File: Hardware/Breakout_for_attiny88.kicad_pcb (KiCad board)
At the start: 2 copper layers, 22.9 x 48.5 mm, 12 parts, among them J1 HEADER, J2 HEADER, J3 AVR-ISP-6, J4 PWR, SW1 SW, U1 ATtiny88

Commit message: add filled zone on both sides.
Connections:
- SW1 pad 3: (no net) -> GND
- SW1 pad 4: (no net) -> GND
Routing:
- net PC6: track 63.4 -> 57.4 mm, vias 0 -> 1
- added copper zone on B.Cu, net GND
- added copper zone on F.Cu, net GND
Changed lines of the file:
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@@
     (property "Sheet name" "")
     (attr through_hole)
-    (fp_text reference "SW1" (at 5.80644 0.0127 90) (layer "F.SilkS")
+    (fp_text reference "SW1" (at 0.48 -3.71 180) (layer "F.SilkS")
       (effects (font (size 1 1) (thickness 0.15)))
     )
@@
       (net 17 "PC6") (pinfunction "2") (solder_mask_margin 0.000254))
     (pad "3" smd rect (at -3.2 -2.075 180) (size 1 1.15) (layers "F.Cu" "F.Paste" "F.Mask")
-      (solder_mask_margin 0.000254))
+      (net 1 "GND") (solder_mask_margin 0.000254))
     (pad "4" smd rect (at 3.2 2.075 180) (size 1 1.15) (layers "F.Cu" "F.Paste" "F.Mask")
-      (solder_mask_margin 0.000254))
+      (net 1 "GND") (solder_mask_margin 0.000254))
     (model "${KISYS3DMOD}/Button_Switch_SMD.3dshapes/SW_SPST_CK_RS282G05A3.wrl"
       (offset (xyz 0 0 0))
@@
     (property "Sheet name" "")
     (attr smd)
-    (fp_text reference "C1" (at 0 1.68 270) (layer "B.SilkS")
+    (fp_text reference "C1" (at 0.965 -2.075) (layer "B.SilkS")
       (effects (font (size 1 1) (thickness 0.15)) (justify mirror))
     )
@@
     (property "Sheet name" "")
     (attr smd)
-    (fp_text reference "R1" (at 0 1.65 180) (layer "B.SilkS")
+    (fp_text reference "R1" (at 3.62 0.01 180) (layer "B.SilkS")
       (effects (font (size 1 1) (thickness 0.15)) (justify mirror))
     )
@@
   (gr_line (start 137.07 77.86518) (end 137.07 126.3868) (layer "Edge.Cuts") (width 0.05))
   (gr_line (start 159.93 77.86518) (end 159.93 126.3868) (layer "Edge.Cuts") (width 0.05))
-  (gr_text "PB3" (at 154.44614 93.62842) (layer "F.SilkS")
-    (effects (font (size 1 1) (thickness 0.15)))
-  )
-  (gr_text "PB2" (at 154.44614 96.16842) (layer "F.SilkS")
-    (effects (font (size 1 1) (thickness 0.15)))
-  )
-  (gr_text "PB1" (at 154.44614 98.70842) (layer "F.SilkS")
-    (effects (font (size 1 1) (thickness 0.15)))
-  )
-  (gr_text "PB0" (at 154.44614 101.24842) (layer "F.SilkS")
-    (effects (font (size 1 1) (thickness 0.15)))
-  )
-  (gr_text "PD7" (at 154.44614 103.78842) (layer "F.SilkS")
-    (effects (font (size 1 1) (thickness 0.15)))
-  )
-  (gr_text "PD6" (at 154.44614 106.32842) (layer "F.SilkS")
-    (effects (font (size 1 1) (thickness 0.15)))
-  )
-  (gr_text "PD5" (at 154.44614 108.86842) (layer "F.SilkS")
-    (effects (font (size 1 1) (thickness 0.15)))
-  )
-  (gr_text "PB7" (at 154.44614 111.40842) (layer "F.SilkS")
-    (effects (font (size 1 1) (thickness 0.15)))
-  )
-  (gr_text "PB6" (at 154.44614 113.94842) (layer "F.SilkS")
-    (effects (font (size 1 1) (thickness 0.15)))
-  )
-  (gr_text "PD4" (at 154.44614 116.48842) (layer "F.SilkS")
-    (effects (font (size 1 1) (thickness 0.15)))
-  )
-  (gr_text "PD3" (at 154.44614 119.02842) (layer "F.SilkS")
-    (effects (font (size 1 1) (thickness 0.15)))
+  (gr_text "PB3" (at 154.63 93.62842) (layer "F.SilkS")
+    (effects (font (size 0.8 0.8) (thickness 0.15)))
+  )
+  (gr_text "PB2" (at 154.63 96.16842) (layer "F.SilkS")
+    (effects (font (size 0.8 0.8) (thickness 0.15)))
+  )
+  (gr_text "PB1" (at 154.63 98.70842) (layer "F.SilkS")
+    (effects (font (size 0.8 0.8) (thickness 0.15)))
+  )
+  (gr_text "PB0" (at 154.63 101.24842) (layer "F.SilkS")
+    (effects (font (size 0.8 0.8) (thickness 0.15)))
+  )
+  (gr_text "PD7" (at 154.63 103.78842) (layer "F.SilkS")
+    (effects (font (size 0.8 0.8) (thickness 0.15)))
+  )
+  (gr_text "PD6" (at 154.63 106.32842) (layer "F.SilkS")
+    (effects (font (size 0.8 0.8) (thickness 0.15)))
+  )
+  (gr_text "PD5" (at 154.63 108.86842) (layer "F.SilkS")
+    (effects (font (size 0.8 0.8) (thickness 0.15)))
+  )
+  (gr_text "PB7" (at 154.63 111.40842) (layer "F.SilkS")
+    (effects (font (size 0.8 0.8) (thickness 0.15)))
+  )
+  (gr_text "PB6" (at 154.63 113.94842) (layer "F.SilkS")
+    (effects (font (size 0.8 0.8) (thickness 0.15)))
+  )
+  (gr_text "PD4" (at 154.63 116.48842) (layer "F.SilkS")
+    (effects (font (size 0.8 0.8) (thickness 0.15)))
+  )
+  (gr_text "PD3" (at 154.63 119.02842) (layer "F.SilkS")
+    (effects (font (size 0.8 0.8) (thickness 0.15)))
   )
   (gr_text "PC2" (at 142.52084 101.41352) (layer "F.SilkS")
@@
     (effects (font (size 1 1) (thickness 0.15)))
   )
-  (gr_text "PB4" (at 154.44614 91.08842) (layer "F.SilkS")
-    (effects (font (size 1 1) (thickness 0.15)))
+  (gr_text "PB4" (at 154.63 91.08842) (layer "F.SilkS")
+    (effects (font (size 0.8 0.8) (thickness 0.15)))
   )
   (segment (start 144.2548 86.6402) (end 144.2548 93.2323) (width 0.2) (layer "F.Cu") (net 1))
@@
   (segment (start 145.82 107.68) (end 147.121142 106.378858) (width 0.2) (layer "F.Cu") (net 17))
   (segment (start 139.61 111.35) (end 142.98 111.35) (width 0.2) (layer "F.Cu") (net 17))
-  (segment (start 138.36 116.97) (end 139 117.61) (width 0.2) (layer "F.Cu") (net 17))
-  (segment (start 139.61 111.35) (end 138.36 112.6) (width 0.2) (layer "F.Cu") (net 17))
-  (segment (start 139 117.61) (end 143.9203 117.61) (width 0.2) (layer "F.Cu") (net 17))
-  (segment (start 138.36 112.6) (end 138.36 116.97) (width 0.2) (layer "F.Cu") (net 17))
-  (segment (start 143.9203 117.61) (end 144.6 116.9303) (width 0.2) (layer "F.Cu") (net 17))
-  (segment (start 144.6 116.9303) (end 144.6 116.03) (width 0.2) (layer "F.Cu") (net 17))
+  (segment (start 142.74 116.03) (end 144.6 116.03) (width 0.2) (layer "F.Cu") (net 17))
+  (via (at 142.74 116.03) (size 0.5) (drill 0.3) (layers "F.Cu" "B.Cu") (net 17))
   (segment (start 143.19 85.165) (end 145.965 82.39) (width 0.2) (layer "B.Cu") (net 17))
   (segment (start 143.19 107.78) (end 143.19 85.165) (width 0.2) (layer "B.Cu") (net 17))
@@
   (segment (start 139.62 111.35) (end 143.19 107.78) (width 0.2) (layer "B.Cu") (net 17))
   (segment (start 139.61 111.35) (end 139.62 111.35) (width 0.2) (layer "B.Cu") (net 17))
+  (segment (start 142.74 114.48) (end 142.74 116.03) (width 0.2) (layer "B.Cu") (net 17))
   (segment (start 147.18 101.96) (end 147.18 102.861) (width 0.2) (layer "B.Cu") (net 17))
   (segment (start 145.811 104.23) (end 143.19 104.23) (width 0.2) (layer "B.Cu") (net 17))
   (segment (start 149.5 99.92) (end 149.5 99.93) (width 0.2) (layer "B.Cu") (net 17))
+  (segment (start 139.61 111.35) (end 142.74 114.48) (width 0.2) (layer "B.Cu") (net 17))
   (segment (start 148.18 101.6779) (end 148.18 101.66) (width 0.2) (layer "F.Cu") (net 18))
   (segment (start 147.7575 102.9847) (end 147.3154 102.5425) (width 0.2) (layer "F.Cu") (net 18))
@@
   (segment (start 145.9372 106.29) (end 146.4847 105.7425) (width 0.2) (layer "F.Cu") (net 29))
   (segment (start 139.61 106.27) (end 139.63 106.29) (width 0.2) (layer "F.Cu") (net 29))
+  (zone (net 1) (net_name "GND") (layer "F.Cu") (name "GroundPlane") (hatch edge 0.508)
+    (connect_pads (clearance 0.508))
+    (min_thickness 0.254) (filled_areas_thickness no)
+    (fill yes (thermal_gap 0.508) (thermal_bridge_width 0.508))
+    (polygon
+      (pts
+        (xy 159.904828 126.361646)
+        (xy 137.095059 126.361702)
+        (xy 137.095171 77.890331)
+        (xy 159.904892 77.890314)
+      )
+    )
+  )
+  (zone (net 1) (net_name "GND") (layer "B.Cu") (name "GroundPlane") (hatch edge 0.508)
+    (connect_pads (clearance 0.508))
+    (min_thickness 0.254) (filled_areas_thickness no)
+    (fill yes (thermal_gap 0.508) (thermal_bridge_width 0.508))
+    (polygon
+      (pts
+        (xy 159.904828 126.35133)
+        (xy 137.095059 126.351386)
+        (xy 137.095171 77.880015)
+        (xy 159.904892 77.879998)
+      )
+    )
+  )
 )

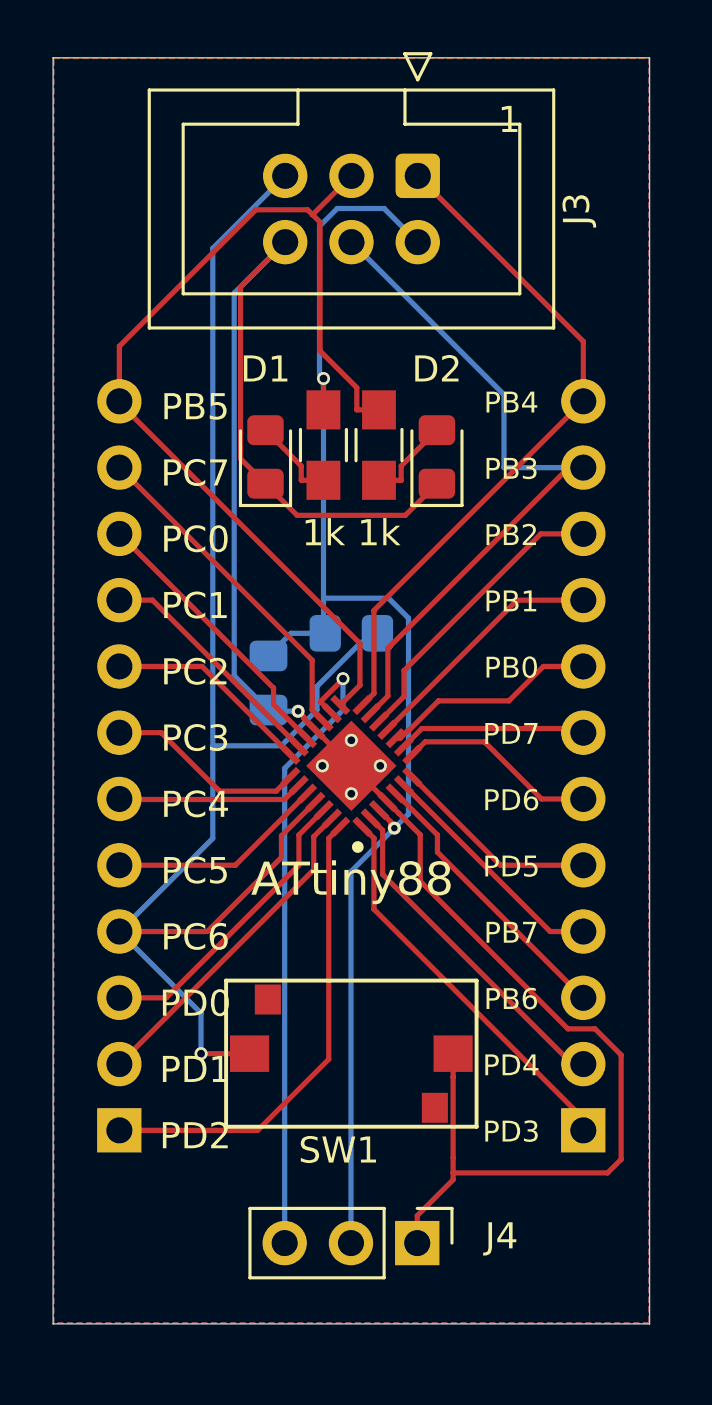
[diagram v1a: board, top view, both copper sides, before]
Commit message: modified Ground plane
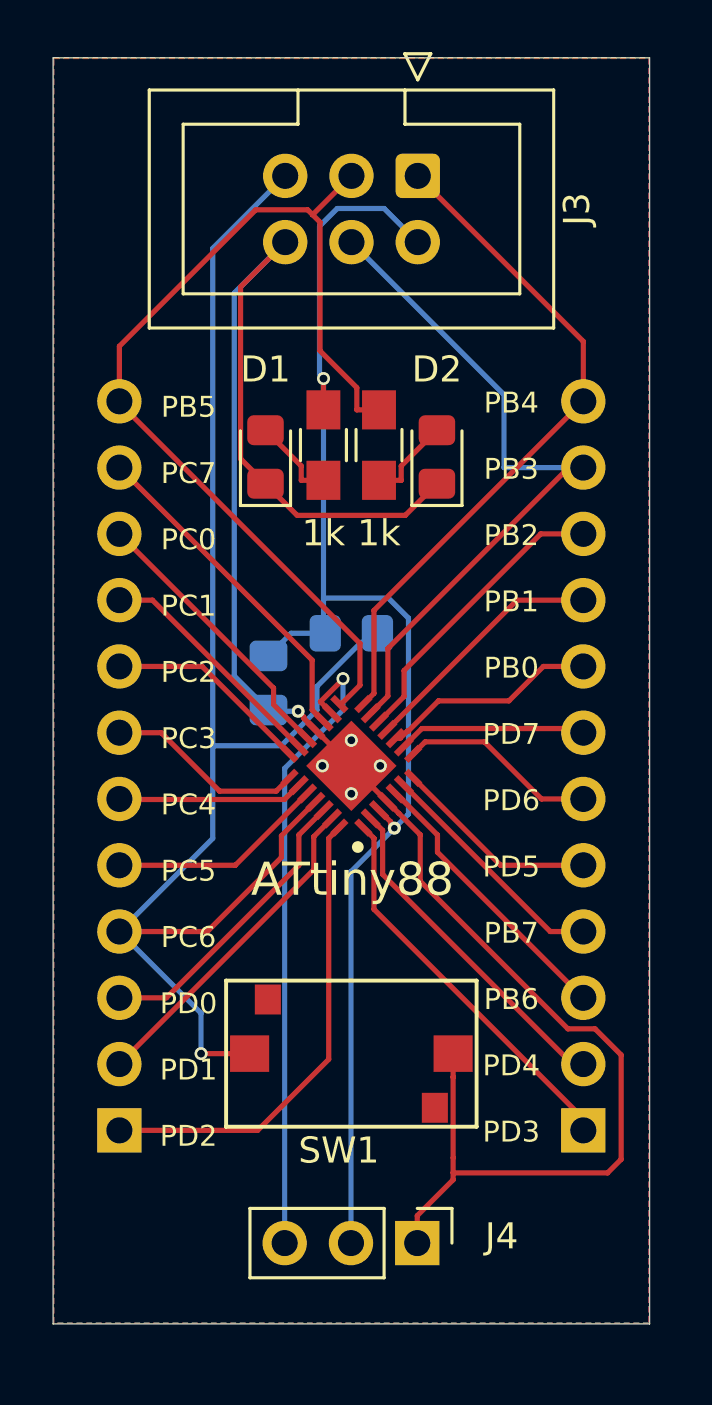
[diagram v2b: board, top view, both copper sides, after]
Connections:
- SW1 pad 4: GND -> (no net)
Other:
- board text removed: "1"
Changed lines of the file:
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@@
   )
   (setup
+    (stackup
+      (layer "F.SilkS" (type "Top Silk Screen"))
+      (layer "F.Paste" (type "Top Solder Paste"))
+      (layer "F.Mask" (type "Top Solder Mask") (color "Green") (thickness 0.01))
+      (layer "F.Cu" (type "copper") (thickness 0.035))
+      (layer "dielectric 1" (type "core") (thickness 1.51) (material "FR4") (epsilon_r 4.5) (loss_tangent 0.02))
+      (layer "B.Cu" (type "copper") (thickness 0.035))
+      (layer "B.Mask" (type "Bottom Solder Mask") (color "Green") (thickness 0.01))
+      (layer "B.Paste" (type "Bottom Solder Paste"))
+      (layer "B.SilkS" (type "Bottom Silk Screen"))
+      (copper_finish "None")
+      (dielectric_constraints no)
+    )
     (grid_origin 148.5 105)
     (pcbplotparams
@@
       (net 1 "GND") (solder_mask_margin 0.000254))
     (pad "4" smd rect (at 3.2 2.075 180) (size 1 1.15) (layers "F.Cu" "F.Paste" "F.Mask")
-      (net 1 "GND") (solder_mask_margin 0.000254))
+      (solder_mask_margin 0.000254))
     (model "${KISYS3DMOD}/Button_Switch_SMD.3dshapes/SW_SPST_CK_RS282G05A3.wrl"
       (offset (xyz 0 0 0))
@@
     )
     (fp_circle (center -2.3745 -2.025) (end -2.3745 -1.9125) (layer "F.SilkS") (width 0.225) (fill none))
+    (fp_line (start -2.625 2.625) (end -2.625 -2.625) (layer "F.CrtYd") (width 0.05))
     (fp_line (start -2.625 -2.625) (end 2.625 -2.625) (layer "F.CrtYd") (width 0.05))
-    (fp_line (start -2.625 2.625) (end -2.625 -2.625) (layer "F.CrtYd") (width 0.05))
     (fp_line (start 2.625 -2.625) (end 2.625 2.625) (layer "F.CrtYd") (width 0.05))
     (fp_line (start 2.625 2.625) (end -2.625 2.625) (layer "F.CrtYd") (width 0.05))
+    (fp_line (start -2 2) (end -2 -2) (layer "F.Fab") (width 0.1))
+    (fp_line (start 2 -2) (end 2 2) (layer "F.Fab") (width 0.1))
+    (fp_line (start -2 -1.55) (end -1.55 -2) (layer "F.Fab") (width 0.1))
     (fp_line (start 2 2) (end -2 2) (layer "F.Fab") (width 0.1))
-    (fp_line (start -2 -1.55) (end -1.55 -2) (layer "F.Fab") (width 0.1))
-    (fp_line (start -2 2) (end -2 -2) (layer "F.Fab") (width 0.1))
     (fp_line (start -2 -2) (end 2 -2) (layer "F.Fab") (width 0.1))
-    (fp_line (start 2 -2) (end 2 2) (layer "F.Fab") (width 0.1))
-    (pad "1" smd rect (at -1.95 -1.35 225) (size 0.25 0.85) (layers "F.Cu" "F.Paste" "F.Mask")
+    (pad "1" smd rect (at -2 -1.35 225) (size 0.25 0.75) (layers "F.Cu" "F.Paste" "F.Mask")
       (net 23 "PD3") (pinfunction "PD3"))
     (pad "2" smd rect (at -1.95 -0.9 225) (size 0.25 0.85) (layers "F.Cu" "F.Paste" "F.Mask")
@@
     (pad "6" smd rect (at -1.95 0.9 225) (size 0.25 0.85) (layers "F.Cu" "F.Paste" "F.Mask")
       (net 9 "PB7") (pinfunction "PB7"))
-    (pad "7" smd rect (at -1.95 1.35 225) (size 0.25 0.85) (layers "F.Cu" "F.Paste" "F.Mask")
+    (pad "7" smd rect (at -2 1.35 225) (size 0.25 0.75) (layers "F.Cu" "F.Paste" "F.Mask")
       (net 21 "PD5") (pinfunction "PD5"))
-    (pad "8" smd rect (at -1.35 1.95 135) (size 0.25 0.85) (layers "F.Cu" "F.Paste" "F.Mask")
+    (pad "8" smd rect (at -1.35 2 135) (size 0.25 0.75) (layers "F.Cu" "F.Paste" "F.Mask")
       (net 20 "PD6") (pinfunction "PD6"))
     (pad "9" smd rect (at -0.9 1.95 135) (size 0.25 0.85) (layers "F.Cu" "F.Paste" "F.Mask")
@@
     (pad "13" smd rect (at 0.9 1.95 135) (size 0.25 0.85) (layers "F.Cu" "F.Paste" "F.Mask")
       (net 13 "MOSI") (pinfunction "PB3"))
-    (pad "14" smd rect (at 1.35 1.95 135) (size 0.25 0.85) (layers "F.Cu" "F.Paste" "F.Mask")
+    (pad "14" smd rect (at 1.35 2 135) (size 0.25 0.75) (layers "F.Cu" "F.Paste" "F.Mask")
       (net 12 "MISO") (pinfunction "PB4"))
-    (pad "15" smd rect (at 1.95 1.35 225) (size 0.25 0.85) (layers "F.Cu" "F.Paste" "F.Mask")
+    (pad "15" smd rect (at 2 1.35 225) (size 0.25 0.75) (layers "F.Cu" "F.Paste" "F.Mask")
       (net 11 "SCK") (pinfunction "PB5"))
     (pad "16" smd rect (at 1.95 0.9 225) (size 0.25 0.85) (layers "F.Cu" "F.Paste" "F.Mask")
@@
     (pad "20" smd rect (at 1.95 -0.9 225) (size 0.25 0.85) (layers "F.Cu" "F.Paste" "F.Mask")
       (net 7 "PC1") (pinfunction "PC1"))
-    (pad "21" smd rect (at 1.95 -1.35 225) (size 0.25 0.85) (layers "F.Cu" "F.Paste" "F.Mask")
+    (pad "21" smd rect (at 2 -1.35 225) (size 0.25 0.75) (layers "F.Cu" "F.Paste" "F.Mask")
       (net 6 "PC2") (pinfunction "PC2"))
-    (pad "22" smd rect (at 1.35 -1.95 135) (size 0.25 0.85) (layers "F.Cu" "F.Paste" "F.Mask")
+    (pad "22" smd rect (at 1.35 -2 135) (size 0.25 0.75) (layers "F.Cu" "F.Paste" "F.Mask")
       (net 5 "PC3") (pinfunction "PC3"))
     (pad "23" smd rect (at 0.9 -1.95 135) (size 0.25 0.85) (layers "F.Cu" "F.Paste" "F.Mask")
@@
     (pad "27" smd rect (at -0.9 -1.95 135) (size 0.25 0.85) (layers "F.Cu" "F.Paste" "F.Mask")
       (net 25 "PD1") (pinfunction "PD1"))
-    (pad "28" smd rect (at -1.35 -1.95 135) (size 0.25 0.85) (layers "F.Cu" "F.Paste" "F.Mask")
+    (pad "28" smd rect (at -1.35 -2 135) (size 0.25 0.75) (layers "F.Cu" "F.Paste" "F.Mask")
       (net 24 "PD2") (pinfunction "PD2"))
     (pad "29" smd rect (at 0 0 135) (size 2.45 2.45) (layers "F.Cu" "F.Paste" "F.Mask")
@@
     (effects (font (size 0.8 0.8) (thickness 0.15)))
   )
-  (gr_text "PC2" (at 142.52084 101.41352) (layer "F.SilkS")
-    (effects (font (size 1 1) (thickness 0.15)))
-  )
-  (gr_text "PC7" (at 142.52084 93.79352) (layer "F.SilkS")
-    (effects (font (size 1 1) (thickness 0.15)))
-  )
-  (gr_text "PC0" (at 142.52084 96.33352) (layer "F.SilkS")
-    (effects (font (size 1 1) (thickness 0.15)))
-  )
-  (gr_text "PC3" (at 142.52084 103.95352) (layer "F.SilkS")
-    (effects (font (size 1 1) (thickness 0.15)))
-  )
-  (gr_text "PC4" (at 142.52084 106.49352) (layer "F.SilkS")
-    (effects (font (size 1 1) (thickness 0.15)))
-  )
-  (gr_text "PC5" (at 142.52084 109.03352) (layer "F.SilkS")
-    (effects (font (size 1 1) (thickness 0.15)))
-  )
-  (gr_text "PC1" (at 142.52084 98.87352) (layer "F.SilkS")
-    (effects (font (size 1 1) (thickness 0.15)))
-  )
-  (gr_text "PC6" (at 142.52084 111.57352) (layer "F.SilkS")
-    (effects (font (size 1 1) (thickness 0.15)))
-  )
-  (gr_text "PD2" (at 142.52084 119.19352) (layer "F.SilkS")
-    (effects (font (size 1 1) (thickness 0.15)))
-  )
-  (gr_text "PD0" (at 142.52084 114.11352) (layer "F.SilkS")
-    (effects (font (size 1 1) (thickness 0.15)))
-  )
-  (gr_text "PD1" (at 142.52084 116.65352) (layer "F.SilkS")
-    (effects (font (size 1 1) (thickness 0.15)))
-  )
-  (gr_text "PB5" (at 142.52084 91.25352) (layer "F.SilkS")
-    (effects (font (size 1 1) (thickness 0.15)))
-  )
-  (gr_text "1" (at 154.55282 80.24516) (layer "F.SilkS")
-    (effects (font (size 1 1) (thickness 0.15)))
+  (gr_text "PC2" (at 142.26 101.41) (layer "F.SilkS")
+    (effects (font (size 0.8 0.8) (thickness 0.15)))
+  )
+  (gr_text "PC7" (at 142.26 93.79) (layer "F.SilkS")
+    (effects (font (size 0.8 0.8) (thickness 0.15)))
+  )
+  (gr_text "PC0" (at 142.26 96.33) (layer "F.SilkS")
+    (effects (font (size 0.8 0.8) (thickness 0.15)))
+  )
+  (gr_text "PC3" (at 142.26 103.95) (layer "F.SilkS")
+    (effects (font (size 0.8 0.8) (thickness 0.15)))
+  )
+  (gr_text "PC4" (at 142.26 106.49) (layer "F.SilkS")
+    (effects (font (size 0.8 0.8) (thickness 0.15)))
+  )
+  (gr_text "PC5" (at 142.26 109.03) (layer "F.SilkS")
+    (effects (font (size 0.8 0.8) (thickness 0.15)))
+  )
+  (gr_text "PC1" (at 142.26 98.87) (layer "F.SilkS")
+    (effects (font (size 0.8 0.8) (thickness 0.15)))
+  )
+  (gr_text "PC6" (at 142.26 111.57) (layer "F.SilkS")
+    (effects (font (size 0.8 0.8) (thickness 0.15)))
+  )
+  (gr_text "PD2" (at 142.26 119.19) (layer "F.SilkS")
+    (effects (font (size 0.8 0.8) (thickness 0.15)))
+  )
+  (gr_text "PD0" (at 142.26 114.11) (layer "F.SilkS")
+    (effects (font (size 0.8 0.8) (thickness 0.15)))
+  )
+  (gr_text "PD1" (at 142.26 116.65) (layer "F.SilkS")
+    (effects (font (size 0.8 0.8) (thickness 0.15)))
+  )
+  (gr_text "PB5" (at 142.26 91.25) (layer "F.SilkS")
+    (effects (font (size 0.8 0.8) (thickness 0.15)))
   )
   (gr_text "PB4" (at 154.63 91.08842) (layer "F.SilkS")

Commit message: Added_New_PCB
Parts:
- added J5: Conn_01x02, Connector_PinHeader_2.54mm:PinHeader_1x02_P2.54mm_Vertical, B.Cu at (139.6, 97.4)
- added J6: Conn_01x02, Connector_PinHeader_2.54mm:PinHeader_1x02_P2.54mm_Vertical, F.Cu at (149.7, 103.0)
- J1, J2: value HEADER -> Conn_01x08; footprint Pin_Headers:Pin_Header_Straight_1x12_Pitch2.54mm -> Connector_PinHeader_2.54mm:PinHeader_1x08_P2.54mm_Vertical
- J3: value AVR-ISP-6 -> Conn_01x08; footprint Connector_IDC:IDC-Header_2x03_P2.54mm_Vertical -> Connector_PinHeader_2.54mm:PinHeader_1x08_P2.54mm_Vertical; moved to B.Cu
- J4: value PWR -> AVR-ISP-6; footprint Pin_Headers:Pin_Header_Straight_1x03_Pitch2.54mm -> Connector_PinHeader_2.54mm:PinHeader_2x03_P2.54mm_Vertical
- SW1: footprint rhydo_labz_switch:rhydolabz_push_button_switch -> rest_switch:push_button_switch
- U1: value ATtiny88 -> ATT88
- moved SW1 31.3 mm to (148.5, 84.7)
- moved J2 26.1 mm to (157.4, 99.9)
- moved J3 25.3 mm to (139.6, 105.0), turned to 180 degrees
- moved R1 8.74 mm to (151.7, 108.1), turned to -90 degrees
- moved U1 7.54 mm to (148.5, 112.5), turned to 0 degrees
- moved C1 6.24 mm to (145.2, 108.1)
- moved J1 3.81 mm to (157.4, 122.8)
- moved D1 2.92 mm to (144.8, 96.0)
- moved R2 2.91 mm to (147.0, 95.6)
- moved D2 2.90 mm to (151.8, 96.1)
- moved R3 2.90 mm to (149.5, 95.6)
- moved J4 1.22 mm to (151.0, 122.1)
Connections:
- J1 pad 1: PD3 -> PB0
- J1 pad 2: PD4 -> PB1
- J1 pad 3: PB6 -> PB2
- J1 pad 4: PB7 -> MOSI
- J1 pad 5: PD5 -> MISO
- J1 pad 6: PD6 -> PB5
- J1 pad 7: PD7 -> PB6
- J1 pad 8: PB0 -> PB7
- J2 pad 1: PD2 -> PC0
- J2 pad 2: PD1 -> PC1
- J2 pad 3: PD0 -> PC2
- J2 pad 4: PC6 -> PC3
- J2 pad 5: PC5 -> PC4
- J2 pad 6: PC4 -> PC5
- J2 pad 7: PC3 -> PC6
- J2 pad 8: PC2 -> PC7
- J3 pad 1: MISO -> PD0
- J3 pad 2: VCC -> PD1
- J3 pad 3: SCK -> PD2
- J3 pad 4: MOSI -> PD3
- J3 pad 5: PC6 -> PD4
- J3 pad 6: GND -> PD5
- J4 pad 1: GND -> MISO
- J4 pad 3: AVCC -> PB5
- R3 pad 1: SCK -> PB5
- SW1 pad 3: GND -> (no net)
- U1 pad 15: SCK -> PB5
- U1 pad 16: AVCC -> VCC
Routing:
- net PB5: track 0.00 -> 47.5 mm, vias 0 -> 1
- net SCK: track 38.7 -> 0.00 mm
- net PC7: track 13.0 -> 38.1 mm
- net AVCC: track 24.4 -> 0.00 mm, vias 1 -> 0
- net GND: track 75.8 -> 97.7 mm, vias 5 -> 3
- net PC5: track 8.33 -> 26.9 mm
- net PC4: track 7.11 -> 24.2 mm
- net VCC: track 53.9 -> 70.8 mm
- net PC3: track 7.71 -> 21.4 mm
- net PC2: track 7.96 -> 19.2 mm
- net PD2: track 18.2 -> 8.13 mm
- net PB7: track 9.20 -> 18.6 mm, vias 0 -> 1
- net PC1: track 9.20 -> 17.5 mm
- net PB6: track 10.8 -> 19.0 mm, vias 0 -> 1
- net PD3: track 15.1 -> 7.45 mm
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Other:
- board size 22.9 x 48.5 mm -> 22.9 x 46.5 mm
- board text added: "+"
- board text added: "1"
- board text added: "5"
- board text added: "GND"
